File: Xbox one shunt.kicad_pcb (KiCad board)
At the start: 2 copper layers, 13.8 x 15 mm, 13 parts, among them U1 INA181A1-Q1, U2 TLV3201AIDCKR

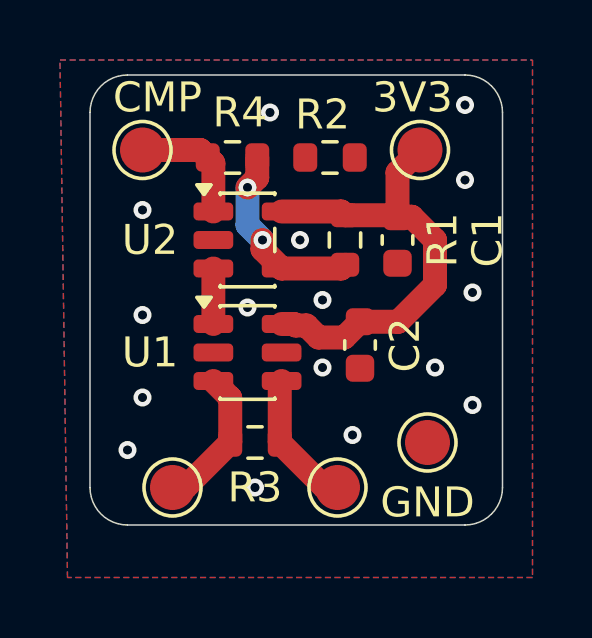
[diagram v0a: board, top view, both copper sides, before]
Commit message: More fixes on the pcb
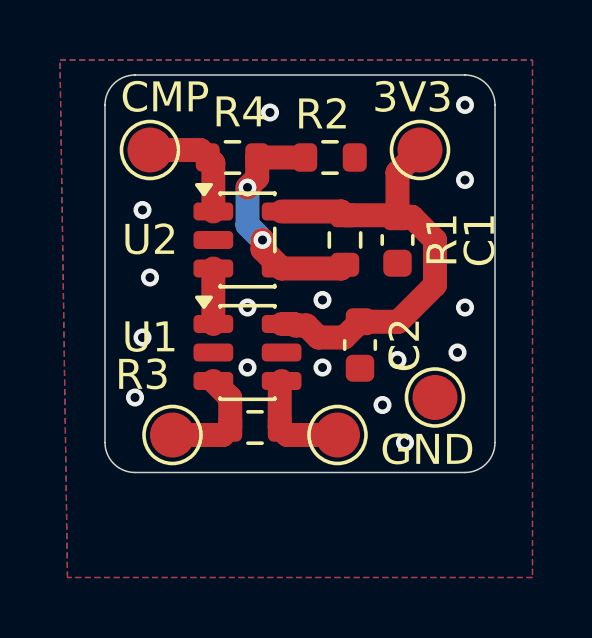
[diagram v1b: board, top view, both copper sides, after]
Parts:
- moved TP2 1.75 mm to (90.8, 105.8)
- moved TP3 1.75 mm to (96.2, 105.8)
- moved GND 1.52 mm to (99.5, 104.5)
- moved R3 0.50 mm to (93.5, 105.5)
- moved CMP 0.25 mm to (90.0, 96.2)
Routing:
- net /VREF: track 6.47 -> 8.07 mm
- net /SHUNT_L: track 4.62 -> 3.60 mm
- net /SHUNT_H: track 4.83 -> 3.81 mm
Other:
- board size 13.8 x 15 mm -> 13 x 13.2 mm
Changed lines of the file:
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@@
 		(tags "SOT TO_SOT_SMD")
 		(property "Reference" "U1"
-			(at -3.25 0 0)
+			(at -3.25 -0.5 0)
 			(layer "F.SilkS")
 			(effects
@@
 	(footprint "Resistor_SMD:R_0603_1608Metric"
 		(layer "F.Cu")
-		(at 93.5 106)
+		(at 93.5 105.5)
 		(descr "Resistor SMD 0603 (1608 Metric), square (rectangular) end terminal, IPC-7351 nominal, (Body size source: IPC-SM-782 page 72, https://www.pcb-3d.com/wordpress/wp-content/uploads/ipc-sm-782a_amendment_1_and_2.pdf), generated with kicad-footprint-generator")
 		(tags "resistor")
 		(property "Reference" "R3"
-			(at 0 1.5 0)
+			(at -3.75 -1.75 0)
 			(layer "F.SilkS")
 			(effects
@@
 	(footprint "TestPoint:TestPoint_Pad_D1.5mm"
 		(layer "F.Cu")
-		(at 89.75 96.25)
+		(at 90 96.25)
 		(descr "SMD pad as test Point, diameter 1.5mm")
 		(tags "test point SMD pad")
@@
 	(footprint "TestPoint:TestPoint_Pad_D1.5mm"
 		(layer "F.Cu")
-		(at 90.75 107.5)
+		(at 90.75 105.75)
 		(descr "SMD pad as test Point, diameter 1.5mm")
 		(tags "test point SMD pad")
@@
 		(tags "capacitor")
 		(property "Reference" "C1"
-			(at 0 3 90)
+			(at 0 2.75 90)
 			(layer "F.SilkS")
 			(effects
@@
 	(footprint "TestPoint:TestPoint_Pad_D1.5mm"
 		(layer "F.Cu")
-		(at 96.25 107.5)
+		(at 96.25 105.75)
 		(descr "SMD pad as test Point, diameter 1.5mm")
 		(tags "test point SMD pad")
@@
 	(footprint "TestPoint:TestPoint_Pad_D1.5mm"
 		(layer "F.Cu")
-		(at 99.25 106)
+		(at 99.5 104.5)
 		(descr "SMD pad as test Point, diameter 1.5mm")
 		(tags "test point SMD pad")
 		(property "Reference" "GND"
-			(at 0 2 0)
+			(at -0.25 1.75 0)
 			(layer "F.SilkS")
 			(effects
@@
 	)
 	(gr_line
-		(start 88 107.5)
-		(end 88 95)
+		(start 88.5 106)
+		(end 88.5 94.75)
 		(stroke
 			(width 0.05)
@@
 	)
 	(gr_arc
-		(start 89.25 108.75)
-		(mid 88.366117 108.383883)
-		(end 88 107.5)
+		(start 89.5 107)
+		(mid 88.792893 106.707107)
+		(end 88.5 106)
 		(stroke
 			(width 0.05)
@@
 		(layer "Edge.Cuts")
 	)
-	(gr_line
+	(gr_arc
 		(start 100.5 93.75)
-		(end 89.25 93.75)
+		(mid 101.207107 94.042893)
+		(end 101.5 94.75)
 		(stroke
 			(width 0.05)
@@
 	)
 	(gr_line
-		(start 101.75 95)
-		(end 101.75 107.5)
+		(start 101.5 94.75)
+		(end 101.5 106)
 		(stroke
 			(width 0.05)
@@
 	)
 	(gr_line
-		(start 100.5 108.75)
-		(end 89.25 108.75)
+		(start 89.5 93.75)
+		(end 100.5 93.75)
 		(stroke
 			(width 0.05)
@@
 	)
 	(gr_arc
-		(start 101.75 107.5)
-		(mid 101.383883 108.383883)
-		(end 100.5 108.75)
+		(start 101.5 106)
+		(mid 101.207107 106.707107)
+		(end 100.5 107)
 		(stroke
 			(width 0.05)
@@
 		(layer "Edge.Cuts")
 	)
-	(gr_arc
-		(start 88 95)
-		(mid 88.366117 94.116117)
-		(end 89.25 93.75)
+	(gr_line
+		(start 100.5 107)
+		(end 89.5 107)
 		(stroke
 			(width 0.05)
@@
 	)
 	(gr_arc
-		(start 100.5 93.75)
-		(mid 101.383883 94.116117)
-		(end 101.75 95)
+		(start 88.5 94.75)
+		(mid 88.792893 94.042893)
+		(end 89.5 93.75)
 		(stroke
 			(width 0.05)
@@
 	)
 	(via
-		(at 89.25 106.25)
-		(size 0.6)
-		(drill 0.3)
-		(layers "F.Cu" "B.Cu")
-		(free yes)
-		(net 2)
-	)
-	(via
-		(at 89.75 104.5)
+		(at 89.75 102.5)
 		(size 0.6)
 		(drill 0.3)
@@
 	)
 	(via
-		(at 96.75 105.75)
-		(size 0.6)
-		(drill 0.3)
-		(layers "F.Cu" "B.Cu")
-		(free yes)
-		(net 2)
-	)
-	(via
-		(at 95 99.25)
+		(at 93.25 103.5)
 		(size 0.6)
 		(drill 0.3)
@@
 	)
 	(via
-		(at 89.75 101.75)
+		(at 90 100.5)
 		(size 0.6)
 		(drill 0.3)
@@
 	)
 	(via
-		(at 93.5 107.5)
+		(at 97.75 104.75)
+		(size 0.6)
+		(drill 0.3)
+		(layers "F.Cu" "B.Cu")
+		(free yes)
+		(net 2)
+	)
+	(via
+		(at 89.5 104.5)
 		(size 0.6)
 		(drill 0.3)
@@
 	)
 	(via
-		(at 100.75 104.75)
+		(at 98.5 106)
 		(size 0.6)
 		(drill 0.3)
@@
 	)
 	(via
-		(at 100.75 101)
+		(at 100.5 101.5)
 		(size 0.6)
 		(drill 0.3)
@@
 	)
 	(via
-		(at 99.5 103.5)
+		(at 98.25 103.25)
+		(size 0.6)
+		(drill 0.3)
+		(layers "F.Cu" "B.Cu")
+		(free yes)
+		(net 2)
+	)
+	(via
+		(at 100.25 103)
 		(size 0.6)
 		(drill 0.3)
@@
 	)
 	(segment
+		(start 93.575 96.5)
+		(end 95.175 96.5)
+		(width 0.8)
+		(layer "F.Cu")
+		(net 3)
+	)
+	(segment
 		(start 93.75 99.5625)
 		(end 94.3875 100.2)
@@
 	)
 	(segment
-		(start 95.825 107.5)
-		(end 94.325 106)
+		(start 96.25 105.75)
+		(end 94.575 105.75)
 		(width 0.8)
 		(layer "F.Cu")
@@
 	)
 	(segment
-		(start 94.325 106)
+		(start 94.325 105.5)
 		(end 94.325 104.0125)
 		(width 0.8)
@@
 	)
 	(segment
-		(start 96.25 107.5)
-		(end 95.825 107.5)
+		(start 94.575 105.75)
+		(end 94.325 105.5)
 		(width 0.8)
 		(layer "F.Cu")
@@
 	)
 	(segment
-		(start 92.675 106)
-		(end 92.675 104.5125)
+		(start 92.425 105.75)
+		(end 92.675 105.5)
 		(width 0.8)
 		(layer "F.Cu")
@@
 	)
 	(segment
-		(start 90.75 107.5)
-		(end 91.175 107.5)
+		(start 92.675 105.5)
+		(end 92.675 104.5125)
 		(width 0.8)
 		(layer "F.Cu")
@@
 	)
 	(segment
-		(start 91.175 107.5)
-		(end 92.675 106)
-		(width 0.8)
-		(layer "F.Cu")
+		(start 90.75 105.75)
+		(end 92.425 105.75)
+		(width 0.8)
+		(layer "F.Cu")

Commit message: quick fixes
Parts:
- moved C2 1.08 mm to (96.6, 103.8)
- moved 3V3 0.97 mm to (99.4, 97.2)
- moved C1 0.97 mm to (98.6, 100.2)
- moved CMP 0.97 mm to (90.4, 97.2)
- moved GND 0.97 mm to (99.9, 105.4)
- moved R1 0.97 mm to (96.9, 100.2)
- moved R2 0.97 mm to (96.4, 97.4)
- moved R4 0.97 mm to (93.1, 97.4)
- moved U1 0.97 mm to (93.6, 103.9)
- moved U2 0.97 mm to (93.6, 100.2)
- moved R3 0.90 mm to (93.6, 106.4)
- moved TP2 0.90 mm to (90.8, 106.7)
- moved TP3 0.90 mm to (96.3, 106.7)
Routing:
- net GND: track 0.00 -> 15.5 mm, vias 16 -> 21
- net +3.3V: track 15.6 -> 15.0 mm
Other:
- board size 13 x 13.2 mm -> 13.5 x 14.2 mm
